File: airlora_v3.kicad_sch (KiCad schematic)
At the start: 0 parts

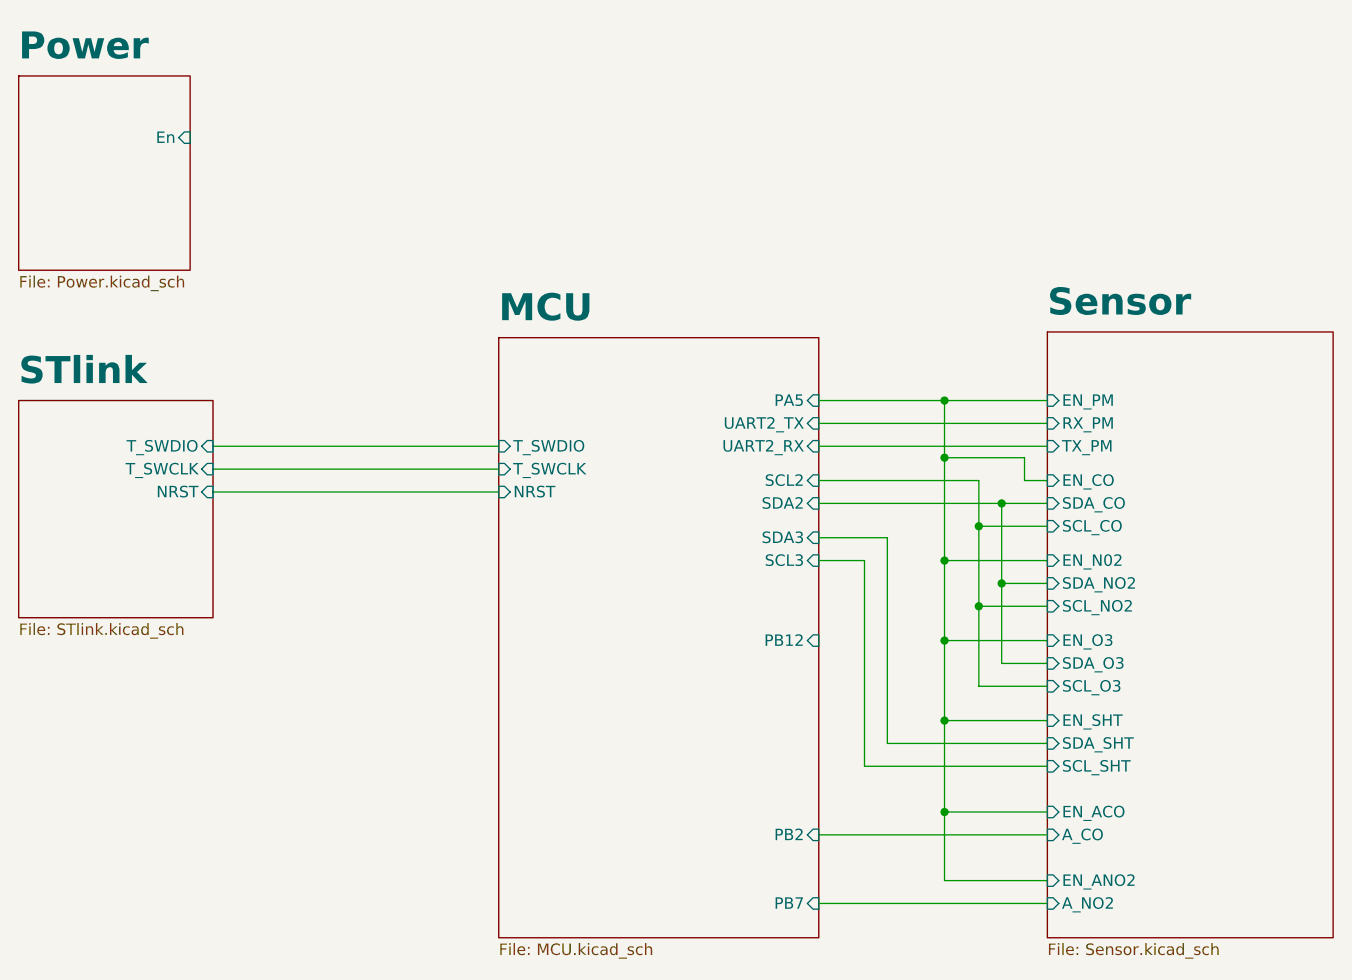
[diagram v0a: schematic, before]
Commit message: Udpate test point
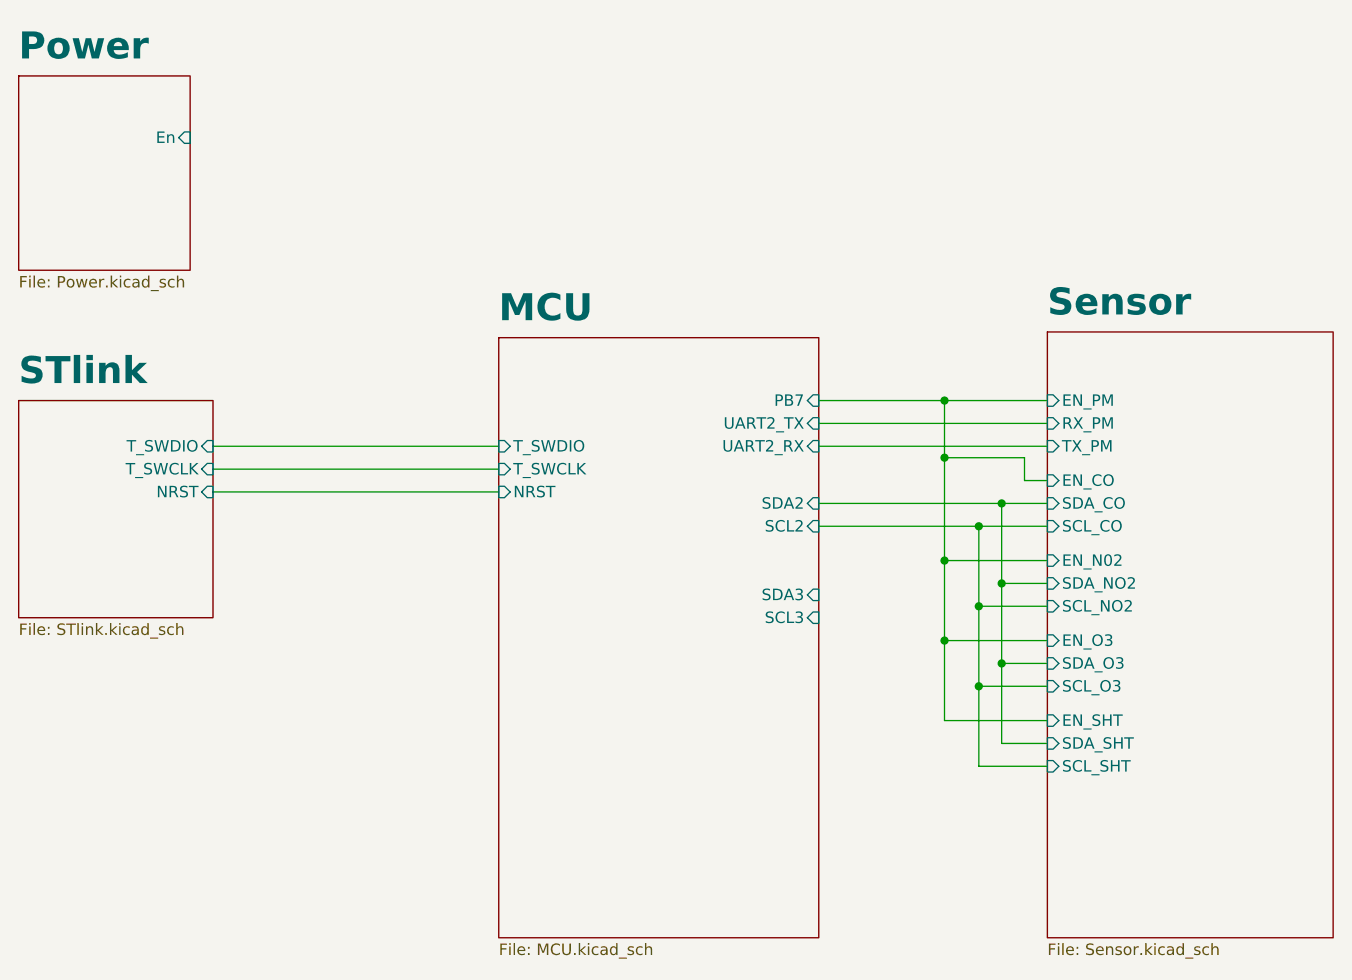
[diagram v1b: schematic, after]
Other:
- sheet MCU ports: added none; removed PA5, PB12, PB2
- sheet Sensor ports: added none; removed A_CO, A_NO2, EN_ACO, EN_ANO2
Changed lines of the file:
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@@
 	)
 	(junction
-		(at 170.18 107.95)
+		(at 176.53 101.6)
+		(diameter 0)
+		(color 0 0 0 0)
+	)
+	(junction
+		(at 173.99 104.14)
+		(diameter 0)
+		(color 0 0 0 0)
+	)
+	(junction
+		(at 170.18 78.74)
 		(diameter 0)
 		(color 0 0 0 0)
@@
 	)
 	(junction
-		(at 170.18 78.74)
+		(at 170.18 72.39)
 		(diameter 0)
 		(color 0 0 0 0)
@@
 	)
 	(junction
-		(at 170.18 118.11)
-		(diameter 0)
-		(color 0 0 0 0)
-	)
-	(junction
-		(at 170.18 72.39)
-		(diameter 0)
-		(color 0 0 0 0)
-	)
-	(junction
 		(at 170.18 99.06)
 		(diameter 0)
@@
 	(wire
 		(pts
-			(xy 156.21 81.28) (xy 173.99 81.28)
-		)
-		(stroke
-			(width 0)
-			(type default)
-		)
-	)
-	(wire
-		(pts
-			(xy 163.83 87.63) (xy 163.83 110.49)
+			(xy 156.21 86.36) (xy 173.99 86.36)
 		)
 		(stroke
@@
 	(wire
 		(pts
+			(xy 156.21 72.39) (xy 170.18 72.39)
+		)
+		(stroke
+			(width 0)
+			(type default)
+		)
+	)
+	(wire
+		(pts
 			(xy 181.61 101.6) (xy 176.53 101.6)
 		)
@@
 	(wire
 		(pts
-			(xy 156.21 72.39) (xy 170.18 72.39)
-		)
-		(stroke
-			(width 0)
-			(type default)
-		)
-	)
-	(wire
-		(pts
-			(xy 156.21 87.63) (xy 163.83 87.63)
-		)
-		(stroke
-			(width 0)
-			(type default)
-		)
-	)
-	(wire
-		(pts
 			(xy 156.21 83.82) (xy 176.53 83.82)
 		)
@@
 	(wire
 		(pts
-			(xy 170.18 118.11) (xy 181.61 118.11)
-		)
-		(stroke
-			(width 0)
-			(type default)
-		)
-	)
-	(wire
-		(pts
 			(xy 173.99 104.14) (xy 173.99 95.25)
 		)
@@
 	(wire
 		(pts
-			(xy 173.99 95.25) (xy 173.99 86.36)
-		)
-		(stroke
-			(width 0)
-			(type default)
-		)
-	)
-	(wire
-		(pts
 			(xy 156.21 77.47) (xy 181.61 77.47)
 		)
@@
 	(wire
 		(pts
-			(xy 156.21 120.65) (xy 181.61 120.65)
-		)
-		(stroke
-			(width 0)
-			(type default)
-		)
-	)
-	(wire
-		(pts
 			(xy 156.21 74.93) (xy 181.61 74.93)
 		)
@@
 	(wire
 		(pts
-			(xy 161.29 90.17) (xy 161.29 113.03)
+			(xy 181.61 110.49) (xy 176.53 110.49)
+		)
+		(stroke
+			(width 0)
+			(type default)
+		)
+	)
+	(wire
+		(pts
+			(xy 173.99 86.36) (xy 173.99 95.25)
 		)
 		(stroke
@@
 	(wire
 		(pts
-			(xy 163.83 110.49) (xy 181.61 110.49)
-		)
-		(stroke
-			(width 0)
-			(type default)
-		)
-	)
-	(wire
-		(pts
 			(xy 170.18 78.74) (xy 170.18 72.39)
 		)
@@
 	(wire
 		(pts
-			(xy 173.99 81.28) (xy 173.99 86.36)
-		)
-		(stroke
-			(width 0)
-			(type default)
-		)
-	)
-	(wire
-		(pts
 			(xy 176.53 83.82) (xy 181.61 83.82)
 		)
@@
 	(wire
 		(pts
-			(xy 170.18 118.11) (xy 170.18 107.95)
+			(xy 173.99 113.03) (xy 173.99 104.14)
+		)
+		(stroke
+			(width 0)
+			(type default)
+		)
+	)
+	(wire
+		(pts
+			(xy 181.61 113.03) (xy 173.99 113.03)
 		)
 		(stroke
@@
 	(wire
 		(pts
-			(xy 156.21 128.27) (xy 181.61 128.27)
+			(xy 176.53 110.49) (xy 176.53 101.6)
 		)
 		(stroke
@@
 	(wire
 		(pts
-			(xy 170.18 125.73) (xy 170.18 118.11)
-		)
-		(stroke
-			(width 0)
-			(type default)
-		)
-	)
-	(wire
-		(pts
 			(xy 176.53 92.71) (xy 176.53 83.82)
 		)
@@
 	(wire
 		(pts
-			(xy 181.61 125.73) (xy 170.18 125.73)
-		)
-		(stroke
-			(width 0)
-			(type default)
-		)
-	)
-	(wire
-		(pts
-			(xy 156.21 90.17) (xy 161.29 90.17)
-		)
-		(stroke
-			(width 0)
-			(type default)
-		)
-	)
-	(wire
-		(pts
 			(xy 181.61 92.71) (xy 176.53 92.71)
-		)
-		(stroke
-			(width 0)
-			(type default)
-		)
-	)
-	(wire
-		(pts
-			(xy 161.29 113.03) (xy 181.61 113.03)
 		)
 		(stroke
@@
 			)
 		)
-		(pin "A_CO" input
-			(at 181.61 120.65 180)
-			(effects
-				(font
-					(size 1.27 1.27)
-				)
-				(justify left)
-			)
-		)
-		(pin "EN_ACO" input
-			(at 181.61 118.11 180)
-			(effects
-				(font
-					(size 1.27 1.27)
-				)
-				(justify left)
-			)
-		)
-		(pin "EN_ANO2" input
-			(at 181.61 125.73 180)
-			(effects
-				(font
-					(size 1.27 1.27)
-				)
-				(justify left)
-			)
-		)
-		(pin "A_NO2" input
-			(at 181.61 128.27 180)
-			(effects
-				(font
-					(size 1.27 1.27)
-				)
-				(justify left)
-			)
-		)
 		(pin "SCL_SHT" input
 			(at 181.61 113.03 180)
@@
 		)
 		(pin "SCL2" input
-			(at 156.21 81.28 0)
+			(at 156.21 86.36 0)
 			(effects
 				(font
@@
 			)
 		)
-		(pin "SDA3" input
-			(at 156.21 87.63 0)
-			(effects
-				(font
-					(size 1.27 1.27)
-				)
-				(justify right)
-			)
-		)
 		(pin "UART2_TX" input
 			(at 156.21 74.93 0)
@@
 			)
 		)
-		(pin "SCL3" input
-			(at 156.21 90.17 0)
-			(effects
-				(font
-					(size 1.27 1.27)
-				)
-				(justify right)
-			)
-		)
 		(pin "NRST" input
 			(at 120.65 82.55 180)
@@
 			)
 		)
-		(pin "PB12" input
-			(at 156.21 99.06 0)
-			(effects
-				(font
-					(size 1.27 1.27)
-				)
-				(justify right)
-			)
-		)
-		(pin "PB2" input
-			(at 156.21 120.65 0)
+		(pin "SDA3" input
+			(at 156.21 93.98 0)
 			(effects
 				(font
@@
 		)
 		(pin "PB7" input
-			(at 156.21 128.27 0)
-			(effects
-				(font
-					(size 1.27 1.27)
-				)
-				(justify right)
-			)
-		)
-		(pin "PA5" input
 			(at 156.21 72.39 0)
 			(effects
 				(font
+					(size 1.27 1.27)
+				)
+				(justify right)
+			)
+		)
+		(pin "SCL3" input
+			(at 156.21 96.52 0)
+			(effects
+				(font

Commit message: Update schemtic
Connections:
- no-connect marks 0 -> 2
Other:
- sheet MCU ports: added UART1_RX, UART1_TX; removed UART2_RX, UART2_TX
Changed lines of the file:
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@@
+	)
+	(junction
+		(at 170.18 81.28)
+		(diameter 0)
+		(color 0 0 0 0)
 	)
 	(junction
@@
 	)
 	(junction
-		(at 170.18 78.74)
-		(diameter 0)
-		(color 0 0 0 0)
-	)
-	(junction
 		(at 176.53 83.82)
 		(diameter 0)
@@
 		(color 0 0 0 0)
 	)
+	(no_connect
+		(at 156.21 93.98)
+	)
+	(no_connect
+		(at 156.21 96.52)
+	)
 	(wire
 		(pts
@@
 	(wire
 		(pts
-			(xy 179.07 78.74) (xy 170.18 78.74)
-		)
-		(stroke
-			(width 0)
-			(type default)
-		)
-	)
-	(wire
-		(pts
 			(xy 170.18 90.17) (xy 181.61 90.17)
 		)
@@
 	(wire
 		(pts
+			(xy 170.18 81.28) (xy 170.18 90.17)
+		)
+		(stroke
+			(width 0)
+			(type default)
+		)
+	)
+	(wire
+		(pts
 			(xy 88.9 82.55) (xy 120.65 82.55)
 		)
@@
 	(wire
 		(pts
-			(xy 170.18 78.74) (xy 170.18 72.39)
-		)
-		(stroke
-			(width 0)
-			(type default)
-		)
-	)
-	(wire
-		(pts
 			(xy 181.61 99.06) (xy 170.18 99.06)
 		)
@@
 	(wire
 		(pts
-			(xy 170.18 78.74) (xy 170.18 90.17)
+			(xy 170.18 72.39) (xy 170.18 81.28)
 		)
 		(stroke
@@
 	(wire
 		(pts
-			(xy 181.61 81.28) (xy 179.07 81.28)
+			(xy 170.18 81.28) (xy 181.61 81.28)
 		)
 		(stroke
@@
 		(pts
 			(xy 170.18 72.39) (xy 181.61 72.39)
-		)
-		(stroke
-			(width 0)
-			(type default)
-		)
-	)
-	(wire
-		(pts
-			(xy 179.07 81.28) (xy 179.07 78.74)
 		)
 		(stroke
@@
 			)
 		)
-		(pin "UART2_TX" input
+		(pin "UART1_TX" input
 			(at 156.21 74.93 0)
 			(effects
@@
 			)
 		)
-		(pin "UART2_RX" input
+		(pin "UART1_RX" input
 			(at 156.21 77.47 0)
 			(effects

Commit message: Update PCB layout
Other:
- sheet MCU ports: added PB3; removed PB7
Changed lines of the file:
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@@
 			)
 		)
-		(pin "PB7" input
-			(at 156.21 72.39 0)
+		(pin "SCL3" input
+			(at 156.21 96.52 0)
 			(effects
 				(font
@@
 			)
 		)
-		(pin "SCL3" input
-			(at 156.21 96.52 0)
+		(pin "PB3" input
+			(at 156.21 72.39 0)
 			(effects
 				(font

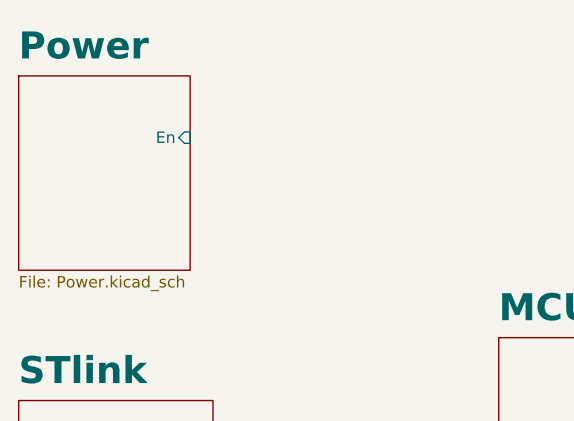
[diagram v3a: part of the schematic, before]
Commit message: Update antenna
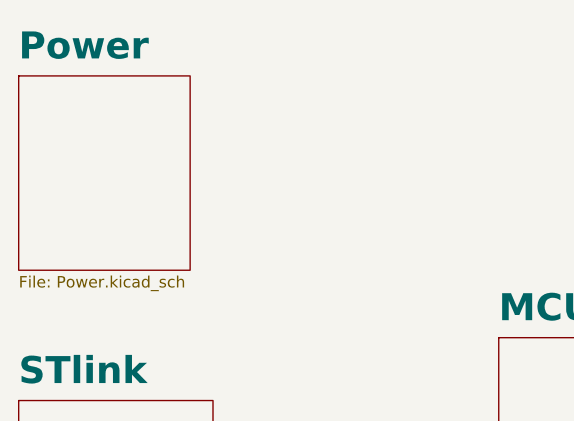
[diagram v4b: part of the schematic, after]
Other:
- sheet Power ports: added none; removed En
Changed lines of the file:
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@@
-			)
-		)
-		(pin "En" input
-			(at 86.36 43.18 0)
-			(effects
-				(font
-					(size 1.27 1.27)
-				)
-				(justify right)
 			)
 		)
